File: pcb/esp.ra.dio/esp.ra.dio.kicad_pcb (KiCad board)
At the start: 2 copper layers, 75 x 28 mm, 34 parts, among them J1 A, J10 UART, J2 B, J3 C, J4 D, J5 START, J6 SELECT, J7 JOY, J8 USB_B_Micro, J9 BATTERY, Q1 BSS138, SW1 POWER, SW2 RESET, SW3 BOOT, U2 VCC, U3 RT9080-33GJ5

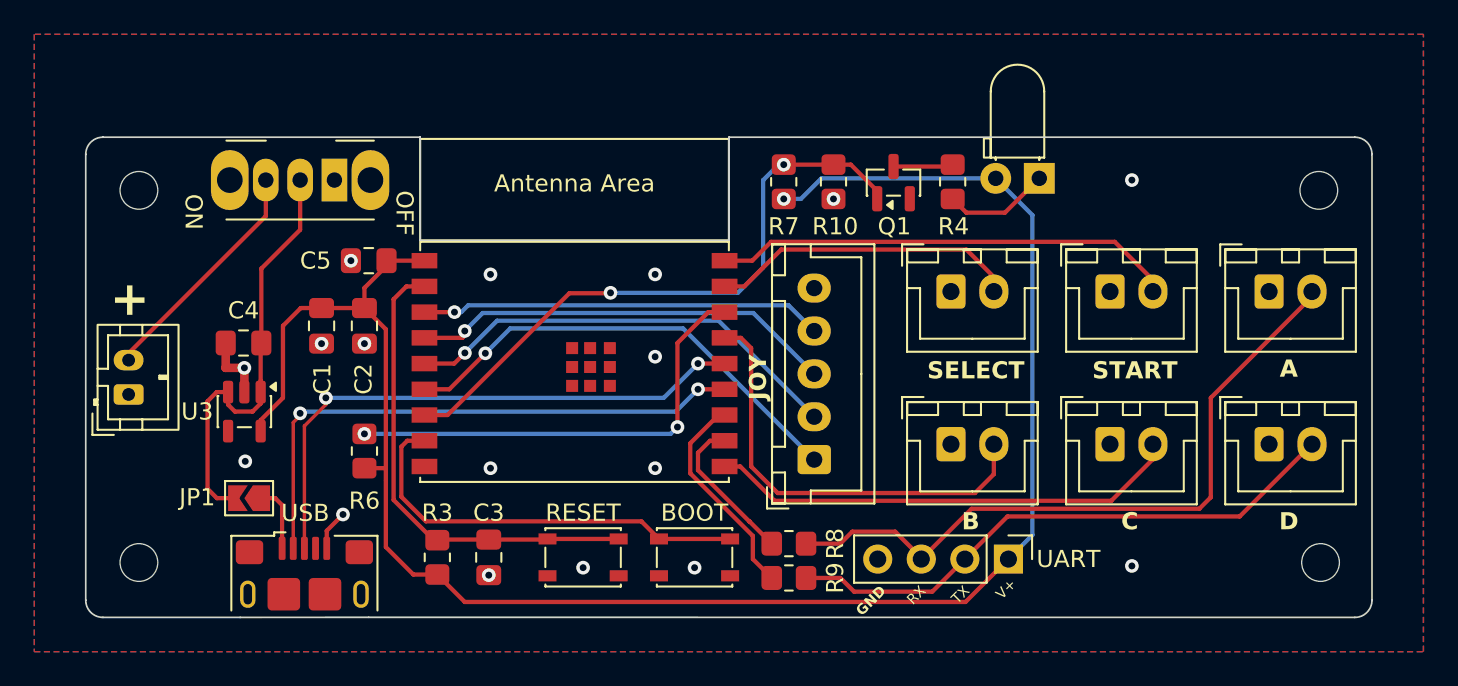
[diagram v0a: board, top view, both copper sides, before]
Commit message: Re-splitting RX/BA nets
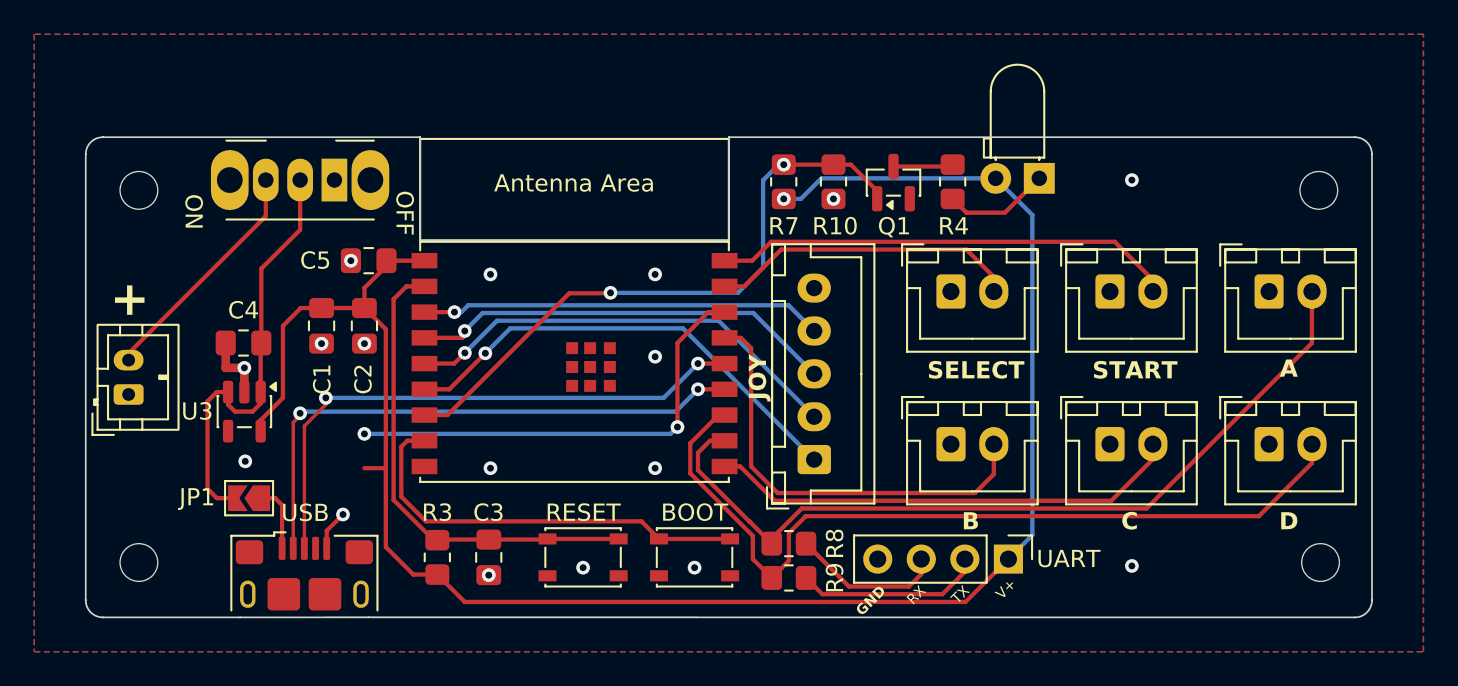
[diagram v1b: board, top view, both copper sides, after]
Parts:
- removed R6: 1M, Resistor_SMD:R_0805_2012Metric_Pad1.20x1.40mm_HandSolder
- R3: value 100K -> 10K
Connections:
- J1 pad 2: /RX/BA -> /BA
- J10 pad 2: /TX/BD -> /TX
- J10 pad 3: /RX/BA -> /RX
- J4 pad 2: /TX/BD -> /BD
- R8 pad 1: Net-(U2-GPIO20/U0RXD) -> /BA
- R8 pad 2: /RX/BA -> /RX
- R9 pad 1: Net-(U2-GPIO21/U0TXD) -> /BD
- R9 pad 2: /TX/BD -> /TX
- U2 pad 11: Net-(U2-GPIO20/U0RXD) -> /BA
- U2 pad 12: Net-(U2-GPIO21/U0TXD) -> /BD
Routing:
- net /BD: track 0.00 -> 48.8 mm
- net /BA: track 0.00 -> 48.5 mm
- net /RX/BA: track 40.5 -> 0.00 mm
- net /TX/BD: track 33.4 -> 0.00 mm
- net Net-(U2-GPIO21/U0TXD): track 12.5 -> 0.00 mm
- net /TX: track 0.00 -> 10.9 mm
- net /RX: track 0.00 -> 8.93 mm
- net Net-(U2-GPIO20/U0RXD): track 8.93 -> 0.00 mm
